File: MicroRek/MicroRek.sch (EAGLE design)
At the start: 41 parts, among them IC3 LSM9DS1TR

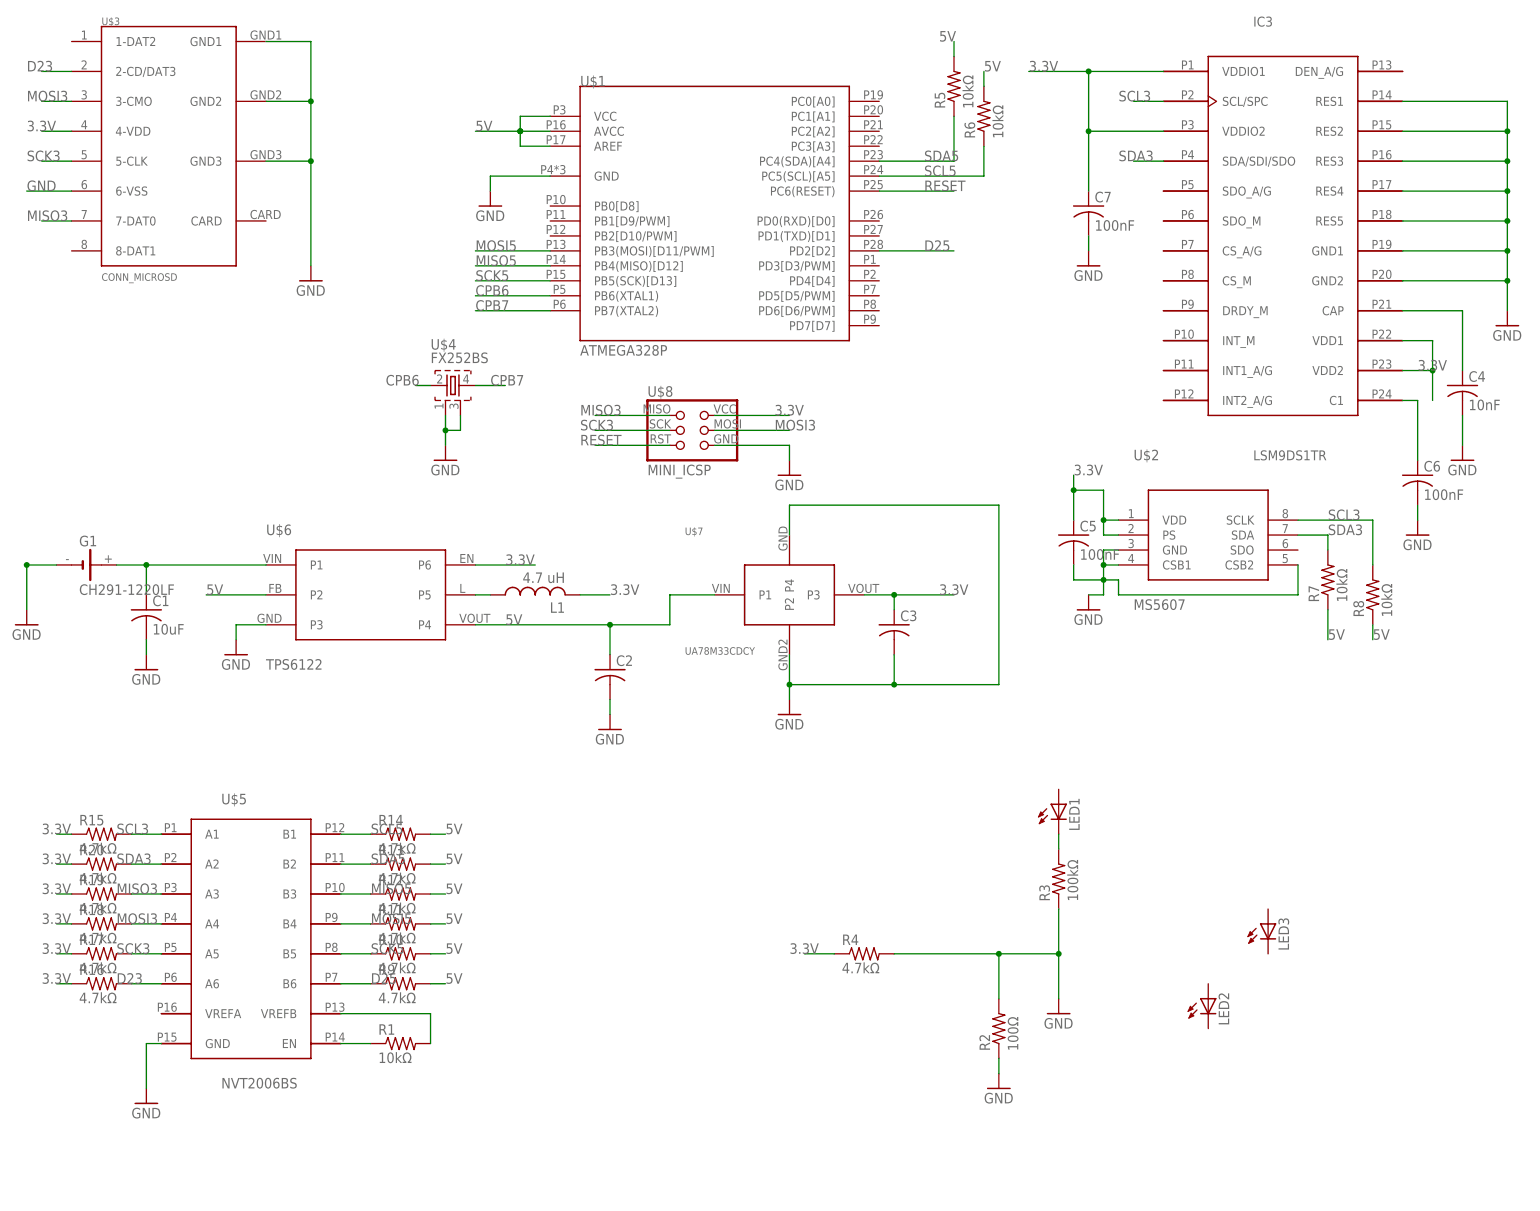
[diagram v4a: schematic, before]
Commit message: Added LED's
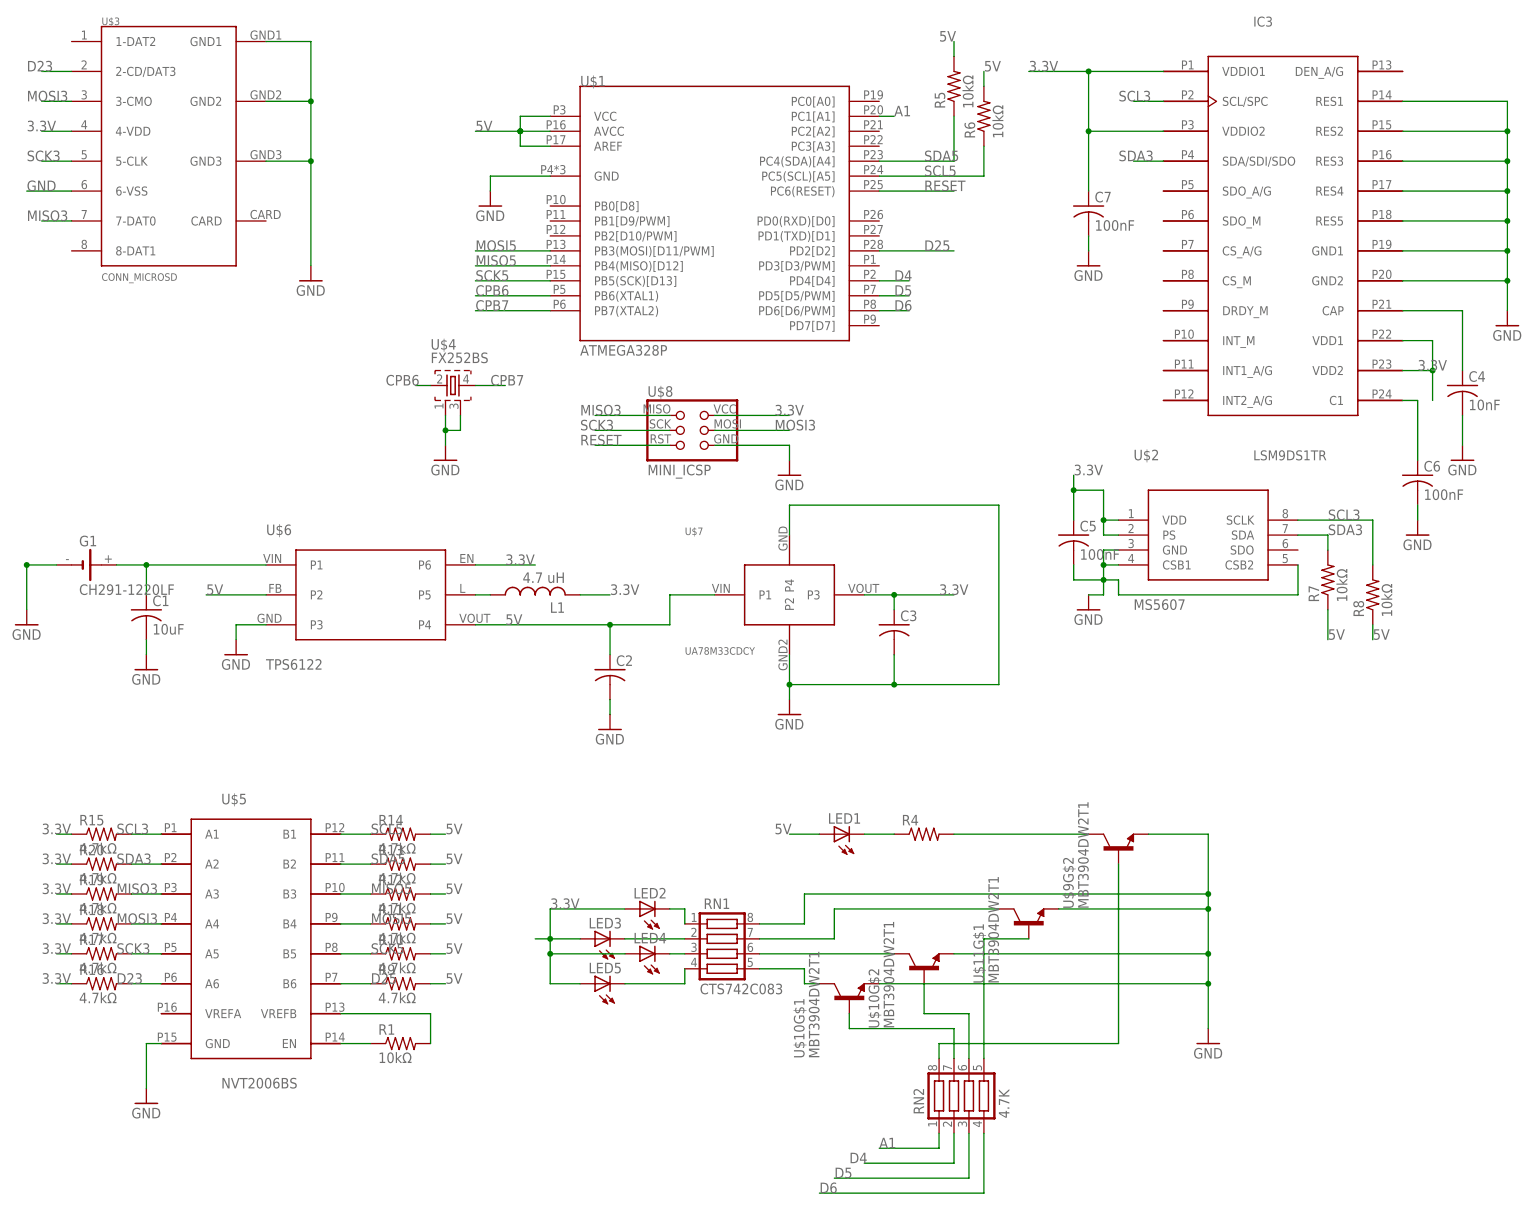
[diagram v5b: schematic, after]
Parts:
- removed R2: 100Ω, resistor:R-US_R0603
- removed R3: 100kΩ, resistor:R-US_R0603
- added LED4, LED5: (no value), led:LEDCHIPLED_0805
- added RN1: CTS742C083, resistor-net:CTS742C083
- added RN2: 4.7K, resistor-net:CTS742C083
- added U$10, U$11, U$9: MBT3904DW2T1, CPSS_IC:MBT3904DW2T1
- R4: value 4.7kΩ -> (none)
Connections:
- removed net N$6: LED1.C, R3.2
- new net A1: RN2.1, U$1.PC1[A1]
- new net D4: RN2.2, U$1.PD4[D4]
- new net D5: RN2.3, U$1.PD5[D5/PWM]
- new net D6: RN2.4, U$1.PD6[D6/PWM]
- new net N$10: LED5.C, RN1.4
- new net N$11: LED4.C, RN1.3
- new net N$12: LED3.C, RN1.2
- new net N$13: LED2.C, RN1.1
- new net N$14: RN2.5, U$11G$1.B
- new net N$15: RN2.8, U$9G$2.B
- new net N$16: RN1.7, U$11G$1.C
- new net N$17: RN2.6, U$10G$2.B
- new net N$18: RN1.6, U$10G$2.C
- new net N$19: RN1.5, U$10G$1.C
- new net N$20: RN2.7, U$10G$1.B
- new net N$7: LED1.C, R4.1
- new net N$8: R4.2, U$9G$2.C
- net 3.3V: now also LED2.A, LED3.A, LED4.A, LED5.A; no longer R4.1
- net 5V: now also LED1.A
- net GND: now also RN1.8, U$10G$1.E, U$10G$2.E, U$11G$1.E, U$9G$2.E; no longer R2.1, R2.2, R3.1, R4.2
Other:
- note removed: "4.7k Pull up on both sides"
- moved on the sheet: LED1, LED2, LED3, R4

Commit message: small led nd pullup update
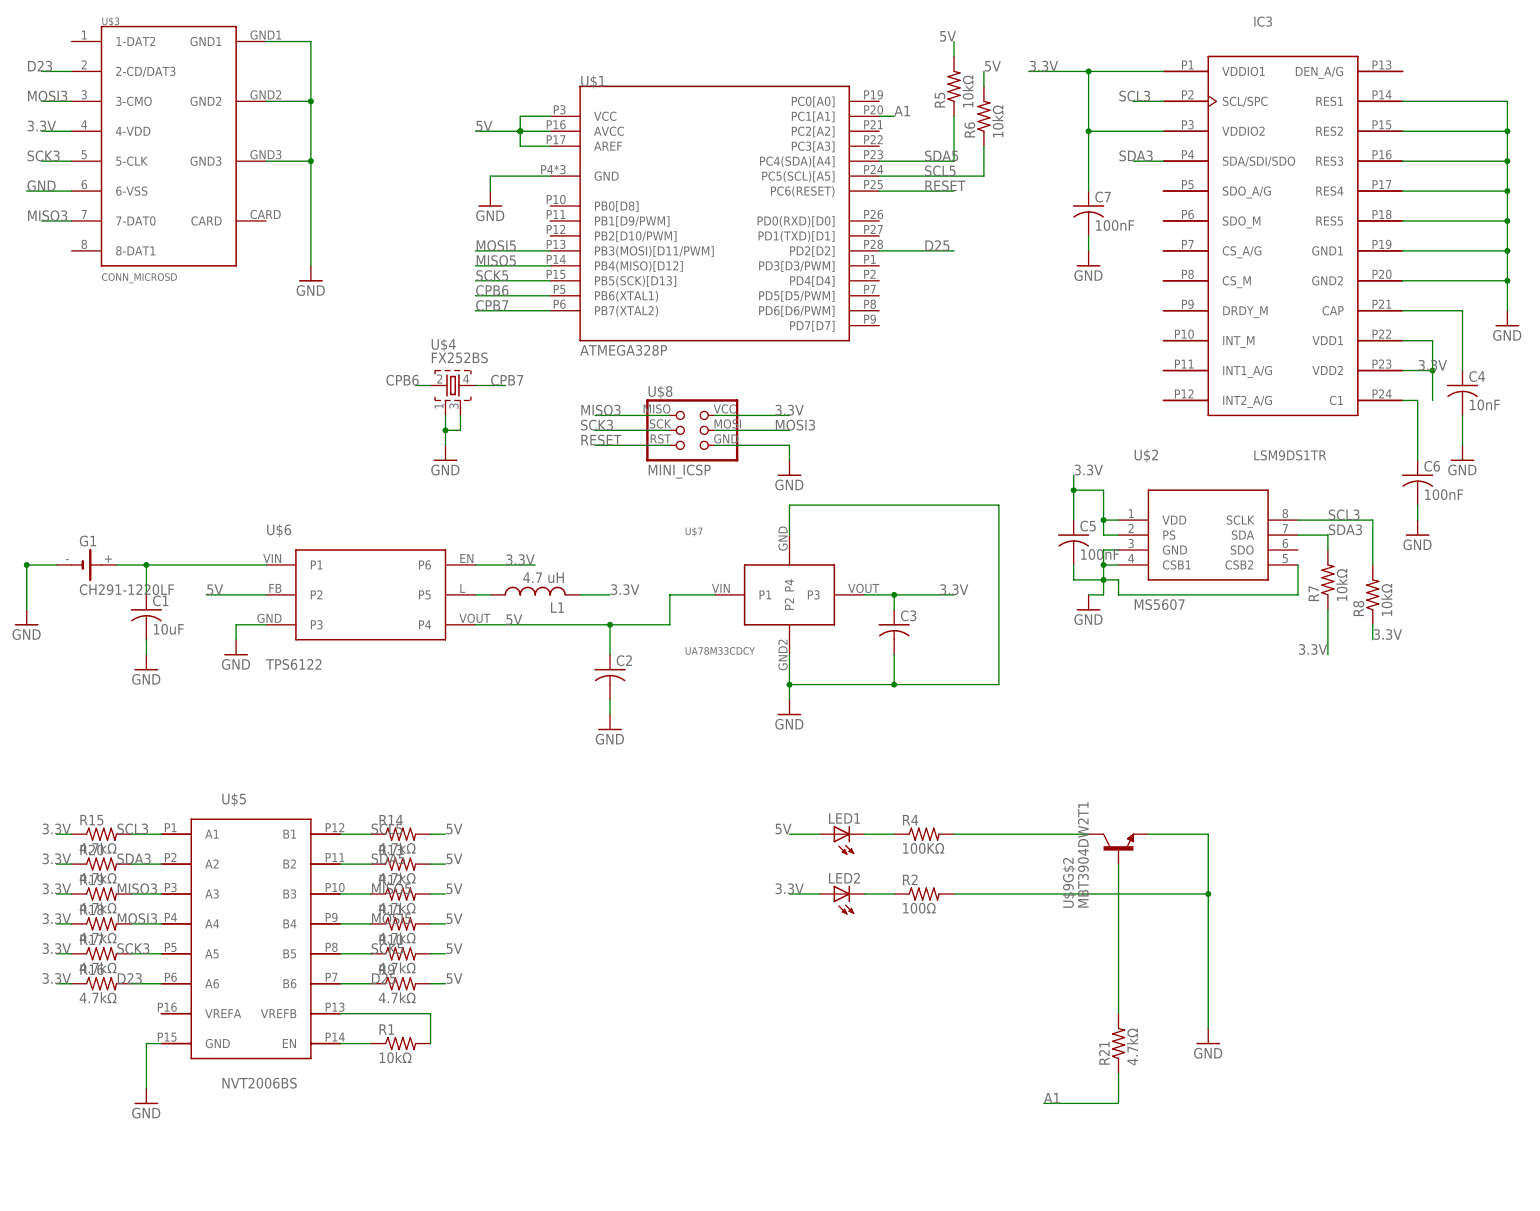
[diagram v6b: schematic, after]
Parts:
- removed LED3, LED4, LED5: (no value), led:LEDCHIPLED_0805
- removed RN1: CTS742C083, resistor-net:CTS742C083
- removed RN2: 4.7K, resistor-net:CTS742C083
- removed U$10, U$11: MBT3904DW2T1, CPSS_IC:MBT3904DW2T1
- added R2: 100Ω, resistor:R-US_R0603
- added R21: 4.7kΩ, resistor:R-US_R0603
- R4: value (none) -> 100KΩ
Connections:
- removed net D4: RN2.2, U$1.PD4[D4]
- removed net D5: RN2.3, U$1.PD5[D5/PWM]
- removed net D6: RN2.4, U$1.PD6[D6/PWM]
- removed net N$10: LED5.C, RN1.4
- removed net N$11: LED4.C, RN1.3
- removed net N$13: LED2.C, RN1.1
- removed net N$14: RN2.5, U$11G$1.B
- removed net N$15: RN2.8, U$9G$2.B
- removed net N$16: RN1.7, U$11G$1.C
- removed net N$17: RN2.6, U$10G$2.B
- removed net N$18: RN1.6, U$10G$2.C
- removed net N$19: RN1.5, U$10G$1.C
- removed net N$20: RN2.7, U$10G$1.B
- new net N$9: LED2.C, R2.1
- net 3.3V: now also R7.1, R8.1; no longer LED3.A, LED4.A, LED5.A
- net 5V: no longer R7.1, R8.1
- net A1: now also R21.1; no longer RN2.1
- net GND: now also R2.2; no longer RN1.8, U$10G$1.E, U$10G$2.E, U$11G$1.E
- net N$12: now also R21.2, U$9G$2.B; no longer LED3.C, RN1.2
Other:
- moved on the sheet: LED2
